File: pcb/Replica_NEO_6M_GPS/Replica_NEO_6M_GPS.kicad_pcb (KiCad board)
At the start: 2 copper layers, 46 x 36 mm, 24 parts, among them J1 CONUFL001-SMD-T, J2 Conn_01x04, U1 TPS79133DBVR, U2 NEO-6M-GPS, U3 24AA32A-I_MS

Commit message: Se hicieron correcciones menores
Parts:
- moved D1 2.15 mm to (159.8, 118.2)
- moved C5 1.90 mm to (159.8, 113.2)
- moved C3 1.82 mm to (155.0, 113.2)
- moved C4 1.82 mm to (155.0, 115.8)
- moved R1 1.82 mm to (155.0, 118.2)
- moved J2 1.25 mm to (134.2, 108.0)
- turned BT1 to 180 degrees
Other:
- board text added: "GND"
- board text added: "RX"
- board text added: "TX"
- board text added: "VCC"
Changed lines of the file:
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@@
   (general
     (thickness 1.6)
-    (drawings 9)
+    (drawings 13)
     (tracks 0)
     (zones 0)
@@
   )
   (module Battery:BatteryHolder_Keystone_2998_1x6.8mm (layer F.Cu)
-    (at 145.5 116)
+    (at 145.5 116 180)
     (descr www.keyelco.com/product-pdf.cfm?p=763)
     (tags "Keystone type 2998 battery holder")
@@
     (fp_arc (start 0 -8.03) (end -2.5 -3.43) (angle -56.6) (layer F.Fab) (width 0.1))
     (fp_arc (start 3.05 -3.15) (end 3.6 -3.44) (angle -125.2183105) (layer F.Fab) (width 0.1))
-    (pad 1 smd rect (at -4.7 0) (size 1.78 5.08) (layers F.Cu F.Paste F.Mask)
+    (pad 1 smd rect (at -4.7 0 180) (size 1.78 5.08) (layers F.Cu F.Paste F.Mask)
       (net 1 "Net-(BT1-Pad1)"))
-    (pad 1 smd rect (at 4.7 0) (size 1.78 5.08) (layers F.Cu F.Paste F.Mask)
+    (pad 1 smd rect (at 4.7 0 180) (size 1.78 5.08) (layers F.Cu F.Paste F.Mask)
       (net 1 "Net-(BT1-Pad1)"))
-    (pad 2 smd rect (at 0 0) (size 3.96 3.96) (layers F.Cu F.Paste F.Mask)
+    (pad 2 smd rect (at 0 0 180) (size 3.96 3.96) (layers F.Cu F.Paste F.Mask)
       (net 2 Earth))
     (model ${KISYS3DMOD}/Battery.3dshapes/BatteryHolder_Keystone_2998_1x6.8mm.wrl
@@
     (tags "capacitor handsolder")
     (attr smd)
-    (fp_text reference C2 (at 0 -1.68) (layer F.SilkS)
+    (fp_text reference C2 (at 2.9625 0) (layer F.SilkS)
       (effects (font (size 1 1) (thickness 0.15)))
     )
@@
   )
   (module Capacitor_SMD:C_0805_2012Metric_Pad1.18x1.45mm_HandSolder (layer F.Cu)
-    (at 154.5 111.5 180)
+    (at 155 113.25 180)
     (descr "Capacitor SMD 0805 (2012 Metric), square (rectangular) end terminal, IPC_7351 nominal with elongated pad for handsoldering. (Body size source: IPC-SM-782 page 76, https://www.pcb-3d.com/wordpress/wp-content/uploads/ipc-sm-782a_amendment_1_and_2.pdf, https://docs.google.com/spreadsheets/d/1BsfQQcO9C6DZCsRaXUlFlo91Tg2WpOkGARC1WS5S8t0/edit?usp=sharing), generated with kicad-footprint-generator")
     (tags "capacitor handsolder")
     (attr smd)
-    (fp_text reference C3 (at 0 -1.68) (layer F.SilkS)
+    (fp_text reference C3 (at 0.25 1.75) (layer F.SilkS)
       (effects (font (size 1 1) (thickness 0.15)))
     )
@@
   )
   (module Capacitor_SMD:C_0805_2012Metric_Pad1.18x1.45mm_HandSolder (layer F.Cu)
-    (at 154.5 114 180)
+    (at 155 115.75 180)
     (descr "Capacitor SMD 0805 (2012 Metric), square (rectangular) end terminal, IPC_7351 nominal with elongated pad for handsoldering. (Body size source: IPC-SM-782 page 76, https://www.pcb-3d.com/wordpress/wp-content/uploads/ipc-sm-782a_amendment_1_and_2.pdf, https://docs.google.com/spreadsheets/d/1BsfQQcO9C6DZCsRaXUlFlo91Tg2WpOkGARC1WS5S8t0/edit?usp=sharing), generated with kicad-footprint-generator")
     (tags "capacitor handsolder")
     (attr smd)
-    (fp_text reference C4 (at 0 -1.68) (layer F.SilkS)
+    (fp_text reference C4 (at -3 0) (layer F.SilkS)
       (effects (font (size 1 1) (thickness 0.15)))
     )
@@
   )
   (module Capacitor_SMD:C_0805_2012Metric_Pad1.18x1.45mm_HandSolder (layer F.Cu)
-    (at 159 111.5)
+    (at 159.75 113.25)
     (descr "Capacitor SMD 0805 (2012 Metric), square (rectangular) end terminal, IPC_7351 nominal with elongated pad for handsoldering. (Body size source: IPC-SM-782 page 76, https://www.pcb-3d.com/wordpress/wp-content/uploads/ipc-sm-782a_amendment_1_and_2.pdf, https://docs.google.com/spreadsheets/d/1BsfQQcO9C6DZCsRaXUlFlo91Tg2WpOkGARC1WS5S8t0/edit?usp=sharing), generated with kicad-footprint-generator")
     (tags "capacitor handsolder")
@@
   (module CONUFL001-SMD-T:LINX_CONUFL001-SMD-T (layer F.Cu)
     (at 174.5 97 270)
-    (fp_text reference J1 (at 0.04 -2.508 90) (layer F.SilkS)
+    (fp_text reference J1 (at 3 -1 180) (layer F.SilkS)
       (effects (font (size 0.8 0.8) (thickness 0.15)))
     )
@@
   )
   (module Connector_PinHeader_2.54mm:PinHeader_1x04_P2.54mm_Horizontal (layer F.Cu)
-    (at 135.5 108 180)
+    (at 134.25 108 180)
     (descr "Through hole angled pin header, 1x04, 2.54mm pitch, 6mm pin length, single row")
     (tags "Through hole angled pin header THT 1x04 2.54mm single row")
-    (fp_text reference J2 (at 4.385 -2.27) (layer F.SilkS)
+    (fp_text reference J2 (at 2 -2.5) (layer F.SilkS)
       (effects (font (size 1 1) (thickness 0.15)))
     )
@@
     (tags "inductor handsolder")
     (attr smd)
-    (fp_text reference L1 (at 0 -1.65 90) (layer F.SilkS)
+    (fp_text reference L1 (at 0 2 180) (layer F.SilkS)
       (effects (font (size 1 1) (thickness 0.15)))
     )
@@
   )
   (module Resistor_SMD:R_0805_2012Metric_Pad1.20x1.40mm_HandSolder (layer F.Cu)
-    (at 154.5 116.5)
+    (at 155 118.25)
     (descr "Resistor SMD 0805 (2012 Metric), square (rectangular) end terminal, IPC_7351 nominal with elongated pad for handsoldering. (Body size source: IPC-SM-782 page 72, https://www.pcb-3d.com/wordpress/wp-content/uploads/ipc-sm-782a_amendment_1_and_2.pdf), generated with kicad-footprint-generator")
     (tags "resistor handsolder")
     (attr smd)
-    (fp_text reference R1 (at 0 -1.65) (layer F.SilkS)
+    (fp_text reference R1 (at 0 1.75) (layer F.SilkS)
       (effects (font (size 1 1) (thickness 0.15)))
     )
@@
     (tags "resistor handsolder")
     (attr smd)
-    (fp_text reference R2 (at 0 -1.65) (layer F.SilkS)
+    (fp_text reference R2 (at 0 1.75) (layer F.SilkS)
       (effects (font (size 1 1) (thickness 0.15)))
     )
@@
     (tags "resistor handsolder")
     (attr smd)
-    (fp_text reference R4 (at 0 -1.65) (layer F.SilkS)
+    (fp_text reference R4 (at -3 0) (layer F.SilkS)
       (effects (font (size 1 1) (thickness 0.15)))
     )
@@
   (module "NEO-6M-GPS d:XCVR_NEO-6M-GPS" (layer F.Cu)
     (at 154.5 97 180)
-    (fp_text reference U2 (at -4.37237 -9.03505) (layer F.SilkS)
+    (fp_text reference U2 (at 6.5 -9) (layer F.SilkS)
       (effects (font (size 0.8 0.8) (thickness 0.15)))
     )
@@
     (tags "diode handsolder")
     (attr smd)
-    (fp_text reference D3 (at 0 -1.65) (layer F.SilkS)
+    (fp_text reference D3 (at -2.975 0) (layer F.SilkS)
       (effects (font (size 1 1) (thickness 0.15)))
     )
@@
     (tags "mounting hole 3mm no annular")
     (attr virtual)
-    (fp_text reference H1 (at 0 -4) (layer F.SilkS)
+    (fp_text reference H1 (at 4.25 -2) (layer F.SilkS)
       (effects (font (size 1 1) (thickness 0.15)))
     )
@@
     (tags "mounting hole 3mm no annular")
     (attr virtual)
-    (fp_text reference H2 (at 0 -4) (layer F.SilkS)
+    (fp_text reference H2 (at -4.25 -2) (layer F.SilkS)
       (effects (font (size 1 1) (thickness 0.15)))
     )
@@
     (tags "mounting hole 3mm no annular")
     (attr virtual)
-    (fp_text reference H3 (at 0 -4) (layer F.SilkS)
+    (fp_text reference H3 (at 1.75 -4) (layer F.SilkS)
       (effects (font (size 1 1) (thickness 0.15)))
     )
@@
     (tags "mounting hole 3mm no annular")
     (attr virtual)
-    (fp_text reference H4 (at 0 -4) (layer F.SilkS)
+    (fp_text reference H4 (at -1.75 -4) (layer F.SilkS)
       (effects (font (size 1 1) (thickness 0.15)))
     )
@@
     (tags "mounting hole 4mm no annular")
     (attr virtual)
-    (fp_text reference H5 (at 0 -5) (layer F.SilkS)
+    (fp_text reference H5 (at 2.75 -5) (layer F.SilkS)
       (effects (font (size 1 1) (thickness 0.15)))
     )
@@
   )
   (module LED_SMD:LED_0805_2012Metric_Pad1.15x1.40mm_HandSolder (layer F.Cu)
-    (at 158.5 116.5 180)
+    (at 159.75 118.25 180)
     (descr "LED SMD 0805 (2012 Metric), square (rectangular) end terminal, IPC_7351 nominal, (Body size source: https://docs.google.com/spreadsheets/d/1BsfQQcO9C6DZCsRaXUlFlo91Tg2WpOkGARC1WS5S8t0/edit?usp=sharing), generated with kicad-footprint-generator")
     (tags "LED handsolder")
     (attr smd)
-    (fp_text reference D1 (at 0 -1.65) (layer F.SilkS)
+    (fp_text reference D1 (at 0 -1.75) (layer F.SilkS)
       (effects (font (size 1 1) (thickness 0.15)))
     )
@@
     (tags "LED handsolder")
     (attr smd)
-    (fp_text reference D2 (at 0 -1.65) (layer F.SilkS)
+    (fp_text reference D2 (at 0 1.75) (layer F.SilkS)
       (effects (font (size 1 1) (thickness 0.15)))
     )
@@
     )
   )
+  (gr_text TX (at 136.75 100.5 90) (layer F.SilkS)
+    (effects (font (size 1 0.7) (thickness 0.15)))
+  )
+  (gr_text RX (at 136.75 103 90) (layer F.SilkS)
+    (effects (font (size 1 0.7) (thickness 0.15)))
+  )
+  (gr_text VCC (at 136.75 105.5 90) (layer F.SilkS)
+    (effects (font (size 1 0.7) (thickness 0.15)))
+  )
+  (gr_text GND (at 136.75 108 90) (layer F.SilkS)
+    (effects (font (size 1 0.7) (thickness 0.15)))
+  )
   (gr_text "- Se incrementaron las dimensiones del PCB respecto al patron dado que se usan footprints mas grandes\n- NOTAS DE CUADRICULA: Borde del PCB (1mm), Margen del PCB (1mm)\n\n" (at 115.5 127.5) (layer Dwgs.User)

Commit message: Se acomodaron archivos y se hicieron retoques
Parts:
- removed BT1: Battery_Cell, Battery:BatteryHolder_Keystone_2998_1x6.8mm
- added B1: MS621FE, MS621FE:MS621FE, F.Cu at (145.2, 115.0)
- moved D1 31.6 mm to (143.0, 91.5)
- moved R1 27.3 mm to (143.0, 93.8)
- moved C4 2.25 mm to (155.0, 118.0)
- moved J2 1.60 mm to (135.5, 107.0)
- moved C5 1.27 mm to (160.0, 114.5)
- moved C3 1.25 mm to (155.0, 114.5)
- moved C2 1.04 mm to (143.0, 104.5)
- moved D3 1.03 mm to (143.0, 107.0)
- moved C1 1.00 mm to (143.0, 96.0)
- moved R4 1.00 mm to (143.0, 109.5)
- moved U1 1.00 mm to (143.0, 100.5)
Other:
- board text added: "Comentarios: - Se incrementaron las dimensiones del PCB respecto al patron dado que se usan footprints mas grandes Bordes y margenes: - Borde de PCB (1 mm) - Margen del PCB (1 mm) Cuadriculas de trabajo: - 0.250 mm para montaje. - 1 mm para dibujo de bordes y margenes"
- board text added: "Diseño Argentina"
- board text added: "FIX"
- board text added: "GPS6MV3"
- board text added: "MS621FE"
- board text added: "PW-LED"
- board text added: "Replica ublox GPS NEO 6M V3 Christian Canaan"
- board text removed: "- Se incrementaron las dimensiones del PCB respecto al patron dado que se usan footprints mas grandes - NOTAS DE CUADRICULA: Borde del PCB (1mm), Margen del PCB (1mm)"

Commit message: Se hicieron correcciones
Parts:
- removed D3: 1N5817, Diode_SMD:D_0805_2012Metric_Pad1.15x1.40mm_HandSolder
- removed R4: 1K, Resistor_SMD:R_0805_2012Metric_Pad1.20x1.40mm_HandSolder
- B1: footprint MS621FE:MS621FE -> foot:MS621FE
- C4: footprint Capacitor_SMD:C_0805_2012Metric_Pad1.18x1.45mm_HandSolder -> foot:CAPC2012X140N
- D1: value LED -> FIX
- D2: value FIX -> 1N5817; footprint LED_SMD:LED_0805_2012Metric_Pad1.15x1.40mm_HandSolder -> Diode_SMD:D_0805_2012Metric_Pad1.15x1.40mm_HandSolder
- J1: footprint CONUFL001-SMD-T:LINX_CONUFL001-SMD-T -> foot:LINX_CONUFL001-SMD-T
- U1: footprint TPS79133DBVR:SOT95P280X145-5N -> foot:SOT95P280X145-5N
- U2: footprint NEO-6M-GPS d:XCVR_NEO-6M-GPS -> foot:XCVR_NEO-6M-GPS
- U3: footprint 24AA32A-I_MS:SOP65P490X110-8N -> foot:SOP65P490X110-8N
- moved D2 45.2 mm to (120.8, 100.2)
- moved R3 44.2 mm to (120.8, 102.8)
- moved J1 28.3 mm to (146.5, 93.0)
- moved L1 27.9 mm to (142.2, 92.2), turned to 90 degrees
- moved R2 27.8 mm to (141.2, 95.5)
- moved H3 27.7 mm to (147.5, 108.5)
- moved H5 26.6 mm to (147.0, 100.5)
- moved C4 26.5 mm to (130.2, 108.5), turned to 0 degrees
- moved C3 26.2 mm to (130.2, 106.0)
- moved H2 26.1 mm to (147.5, 87.5)
- moved C5 24.9 mm to (135.8, 108.5)
- moved C2 23.3 mm to (120.8, 97.8), turned to 0 degrees
- moved U1 23.1 mm to (120.8, 94.2)
- moved C1 22.9 mm to (120.8, 90.8), turned to 180 degrees
- moved U2 22.8 mm to (131.8, 95.2)
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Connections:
- net /Modulo GPS/RXD1 renamed /RXD1
- net /Modulo GPS/SCL2 renamed /SCL2
- net /Modulo GPS/SDA2 renamed /SDA2
- B1 pad -: Earth -> GND
- C1 pad 1: /Regulador de voltaje lineal de potencia/+5V -> VCC
- C1 pad 2: Earth -> GND
- C2 pad 2: Earth -> GND
- C3 pad 1: /Modulo GPS/3.3V -> +3V3
- C3 pad 2: Earth -> GND
- C4 pad 1: /Modulo GPS/3.3V -> GND
- C4 pad 2: Earth -> +3V3
- C5 pad 1: /Modulo GPS/3.3V -> +3V3
- C5 pad 2: Earth -> GND
- D1 pad 1: Earth -> GND
- D2 pad 1: Earth -> Net-(D2-Pad1)
- D2 pad 2: Net-(D2-Pad2) -> +3V3
- J1 pad 2: Earth -> GND
- J1 pad 3: Earth -> GND
- J2 pad 1: Earth -> VCC
- J2 pad 2: /Regulador de voltaje lineal de potencia/+5V -> /TXD1
- J2 pad 4: /Modulo GPS/TXD1 -> GND
- R1 pad 1: /Modulo GPS/3.3V -> Net-(R1-Pad1)
- R3 pad 1: Net-(R3-Pad1) -> Net-(D2-Pad1)
- R3 pad 2: Net-(D2-Pad2) -> Net-(B1-Pad+)
- U1 pad 1: /Regulador de voltaje lineal de potencia/+5V -> VCC
- U1 pad 2: Earth -> GND
- U1 pad 3: Earth -> GND
- U1 pad 5: /Modulo GPS/3.3V -> +3V3
- U2 pad 10: Earth -> GND
- U2 pad 12: Earth -> GND
- U2 pad 13: Earth -> GND
- U2 pad 20: /Modulo GPS/TXD1 -> /TXD1
- U2 pad 23: /Modulo GPS/3.3V -> +3V3
- U2 pad 24: Earth -> GND
- U2 pad 3: Net-(R3-Pad1) -> Net-(R1-Pad1)
- U2 pad 7: Earth -> GND
- U3 pad 1: Earth -> GND
- U3 pad 2: Earth -> GND
- U3 pad 3: Earth -> GND
- U3 pad 4: Earth -> GND
- U3 pad 7: Earth -> GND
- U3 pad 8: /Modulo GPS/3.3V -> +3V3
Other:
- board size 46 x 36 mm -> 36 x 26 mm
- board text added: "Comentarios: - No encuentro el footprint apropiado para la bateria, los que encuentro son mas grandes y no entran en el pcb (ademas de que no se corresponden con la pila que debe ir alli) Bordes y margenes: - Borde de PCB (1 mm) - Margen del PCB (1 mm) Cuadriculas de trabajo: - 0.250 mm para montaje. - 1 mm para dibujo de bordes y margenes"
- board text added: "Replica uBLOX NEO-6M GPS Module DCI - 3CEIoT UBA Christian Canaan UBA - Argentina"
- board text removed: "Comentarios: - Se incrementaron las dimensiones del PCB respecto al patron dado que se usan footprints mas grandes Bordes y margenes: - Borde de PCB (1 mm) - Margen del PCB (1 mm) Cuadriculas de trabajo: - 0.250 mm para montaje. - 1 mm para dibujo de bordes y margenes"
- board text removed: "FIX"
- board text removed: "GPS6MV3"
- board text removed: "MS621FE"
- board text removed: "PW-LED"
- board text removed: "Replica ublox GPS NEO 6M V3 Christian Canaan"

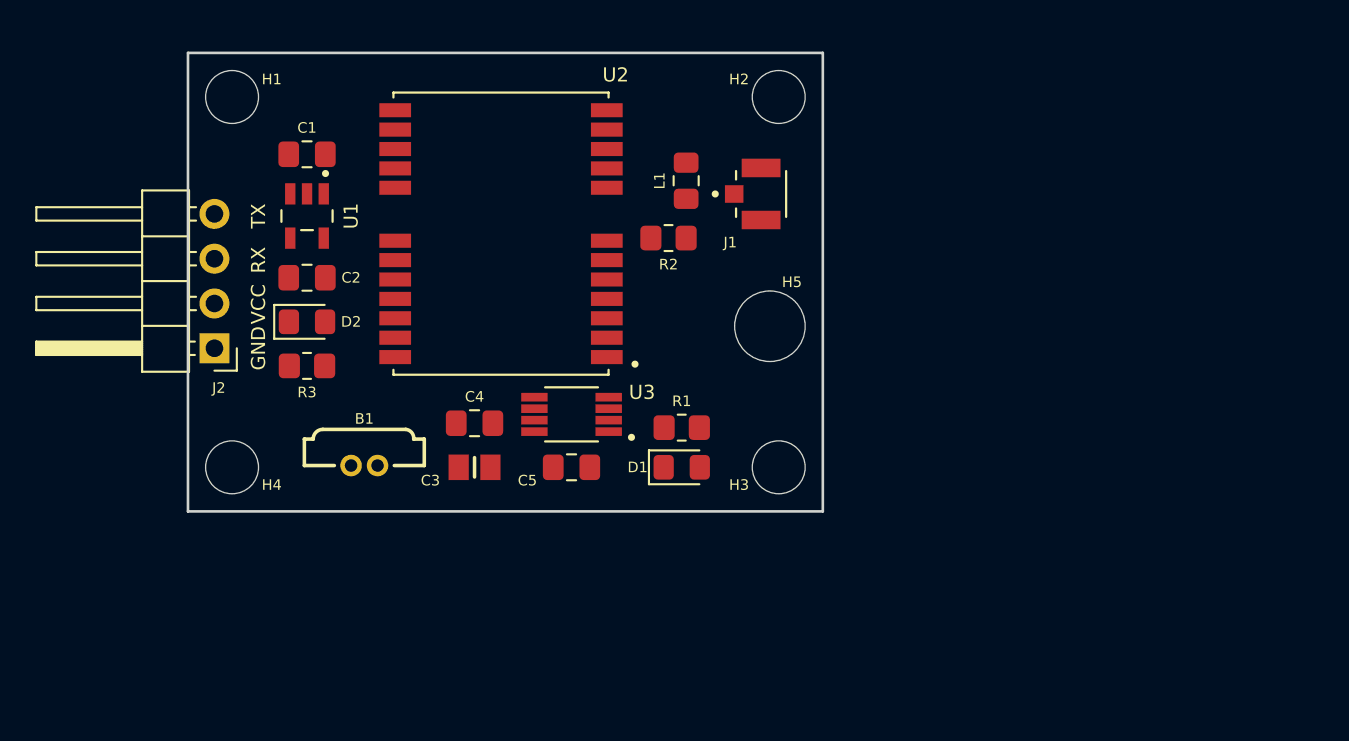
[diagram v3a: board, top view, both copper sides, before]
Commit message: Se acomodaron directorios y se hicieron correcciones
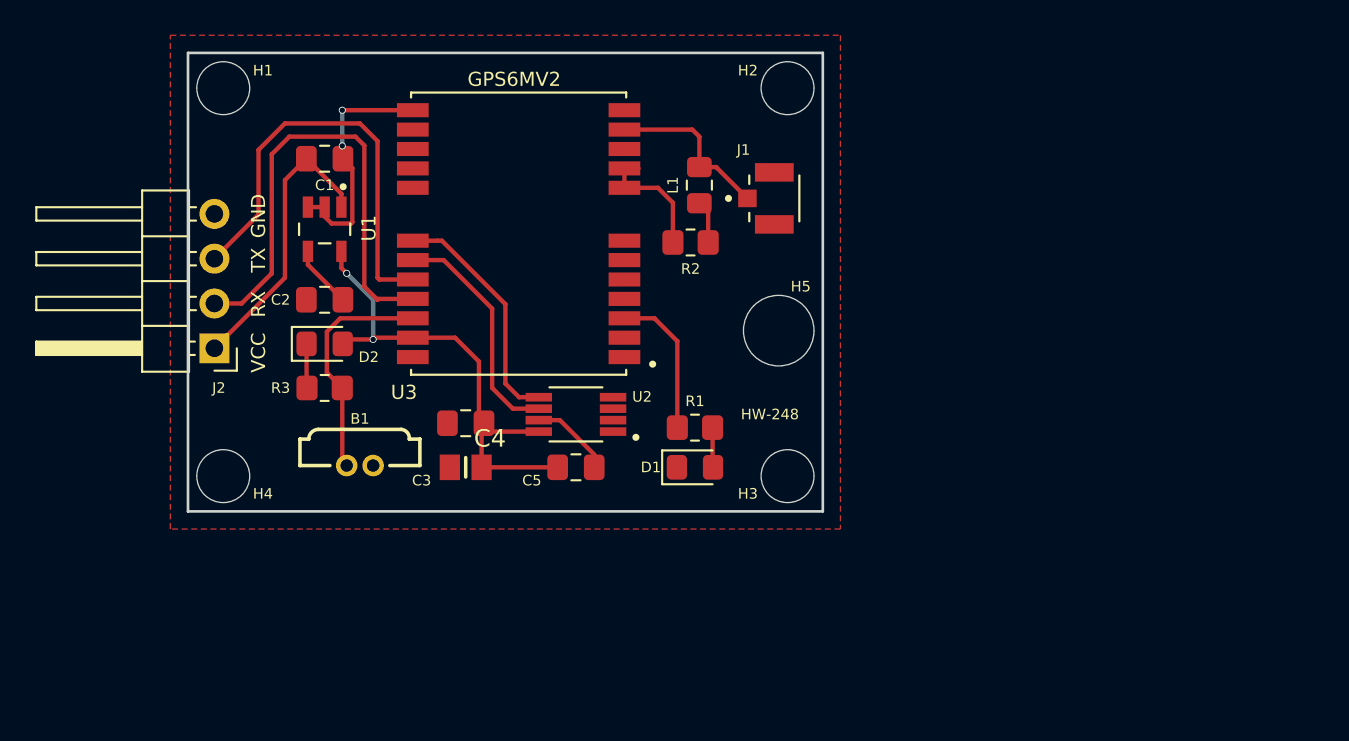
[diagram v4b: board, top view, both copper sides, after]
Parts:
- C4: value 4.7uF -> TAJP156M006SNJ
- U2: value NEO-6M-GPS -> 24AA32A-I_MS; footprint foot:XCVR_NEO-6M-GPS -> foot:SOP65P490X110-8N
- U3: value 24AA32A-I_MS -> NEO-6M-GPS; footprint foot:SOP65P490X110-8N -> foot:XCVR_NEO-6M-GPS
- moved U2 11.1 mm to (136.0, 105.5)
- moved U3 10.7 mm to (132.8, 95.2)
- moved C2 1.60 mm to (121.8, 99.0), turned to 180 degrees
- moved D2 1.60 mm to (121.8, 101.5)
- moved R3 1.60 mm to (121.8, 104.0)
- moved R2 1.27 mm to (142.5, 95.8)
- moved U1 1.25 mm to (121.8, 95.0)
- moved C1 1.03 mm to (121.8, 91.0), turned to 0 degrees
- moved J1 0.79 mm to (147.2, 93.2)
- moved L1 0.79 mm to (143.0, 92.5), turned to 270 degrees
- moved D1 0.75 mm to (142.8, 108.5)
- moved R1 0.75 mm to (142.8, 106.2)
- moved H1 0.71 mm to (116.0, 87.0)
- moved H2 0.71 mm to (148.0, 87.0)
- moved H3 0.71 mm to (148.0, 109.0)
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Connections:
- J2 pad 2: /TXD1 -> /RXD1
- J2 pad 3: /RXD1 -> /TXD1
- U2 pad 1: Net-(U2-Pad1) -> GND
- U2 pad 2: Net-(U2-Pad2) -> GND
- U2 pad 3: Net-(R1-Pad1) -> GND
- U2 pad 4: Net-(U2-Pad4) -> GND
- U2 pad 5: Net-(U2-Pad5) -> /SDA2
- U2 pad 6: Net-(U2-Pad6) -> /SCL2
- U2 pad 8: Net-(R2-Pad1) -> +3V3
- U3 pad 1: GND -> Net-(U3-Pad1)
- U3 pad 2: GND -> Net-(U3-Pad2)
- U3 pad 3: GND -> Net-(R1-Pad1)
- U3 pad 4: GND -> Net-(U3-Pad4)
- U3 pad 5: /SDA2 -> Net-(U3-Pad5)
- U3 pad 6: /SCL2 -> Net-(U3-Pad6)
- U3 pad 8: +3V3 -> Net-(R2-Pad1)
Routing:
- net +3V3: track 0.00 -> 28.0 mm, vias 0 -> 2
- net /RXD1: track 0.00 -> 27.7 mm
- net /TXD1: track 0.00 -> 24.8 mm
- net GND: track 0.00 -> 19.0 mm, vias 0 -> 2
- net VCC: track 0.00 -> 16.5 mm
- net /SDA2: track 0.00 -> 13.5 mm
- net /SCL2: track 0.00 -> 13.3 mm
- net Net-(B1-Pad+): track 0.00 -> 13.2 mm
- net Net-(J1-Pad1): track 0.00 -> 9.25 mm
- net Net-(R1-Pad1): track 0.00 -> 8.44 mm
- net Net-(R2-Pad1): track 0.00 -> 7.25 mm
- net Net-(C2-Pad1): track 0.00 -> 4.33 mm
- net Net-(D2-Pad1): track 0.00 -> 2.51 mm
- net Net-(L1-Pad2): track 0.00 -> 2.43 mm
- net Net-(D1-Pad2): track 0.00 -> 2.26 mm
- added copper zone on F.Cu, net GND
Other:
- net class Default: via_dia 0.8 -> 0.4; via_drill 0.4 -> 0.3
- board text added: "Comentarios: - No encuentro el footprint apropiado para la bateria, los que encuentro son mas grandes y no entran en el pcb (ademas de que no se corresponden con la pila que debe ir alli) - Fue muy complicado el ruteo sobre U1, el unico modelo que encontre esta espejado respecto a la replica y eso me obligo a usar la otra capa y armar puentes. Bordes y margenes: - Borde de PCB (1 mm) - Margen del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"
- board text added: "GPS6MV2"
- board text added: "HW-248"
- board text removed: "Comentarios: - No encuentro el footprint apropiado para la bateria, los que encuentro son mas grandes y no entran en el pcb (ademas de que no se corresponden con la pila que debe ir alli) Bordes y margenes: - Borde de PCB (1 mm) - Margen del PCB (1 mm) Cuadriculas de trabajo: - 0.250 mm para montaje. - 1 mm para dibujo de bordes y margenes"
